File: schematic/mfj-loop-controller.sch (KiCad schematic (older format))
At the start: 35 parts, among them J1 Adafruit ADS1115, J2 Bias Tee, J3 SWR Bridge, J4 DC+12V, U1 AD8032, U2 R-785.0-1.0, U3 TMR3-1212, U4 WeMos_D1_mini, U5 LCC120, U6 LCC120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

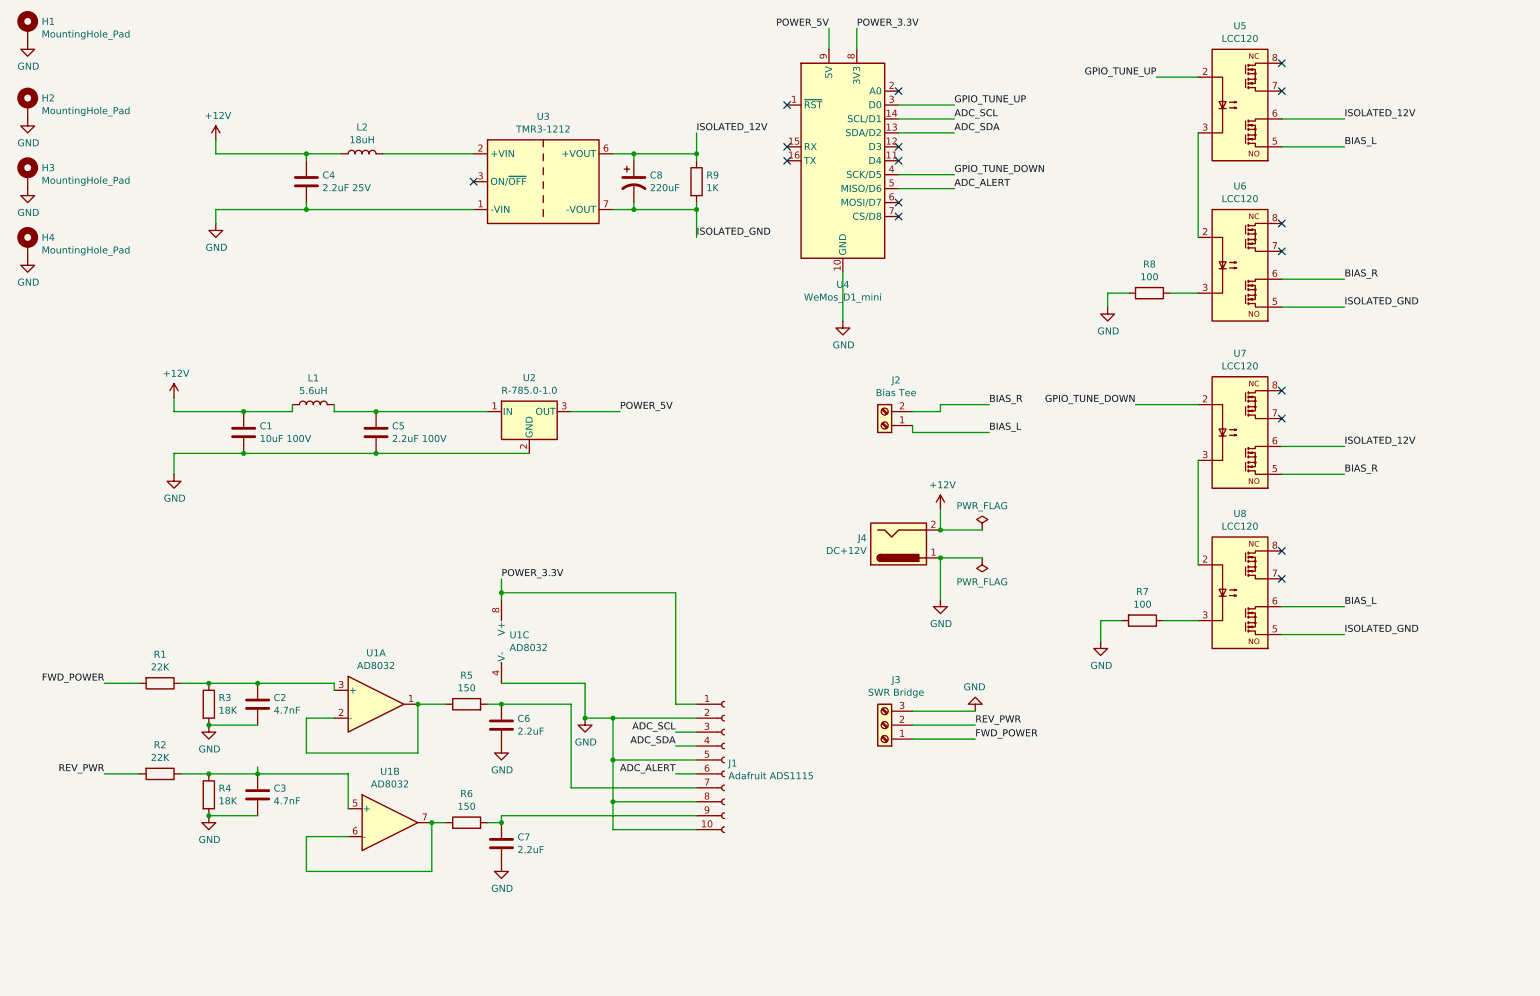
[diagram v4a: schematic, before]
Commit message: Hardware version 1.2.0:
1. Change 12V isolated supply to "low ripple/noise" version (TVN 3-1212).
2. Add/update required filtering to reflect TVN 3-1212 and to further reduce ripple.
3. Reroute isolated section to shorten traces and to use isolated power/ground planes (EMI reduction).
4. Add optional (?) "minimum load" resistors for use if TVN 3-1212 requires them for proper operation while idle/slow tuning.
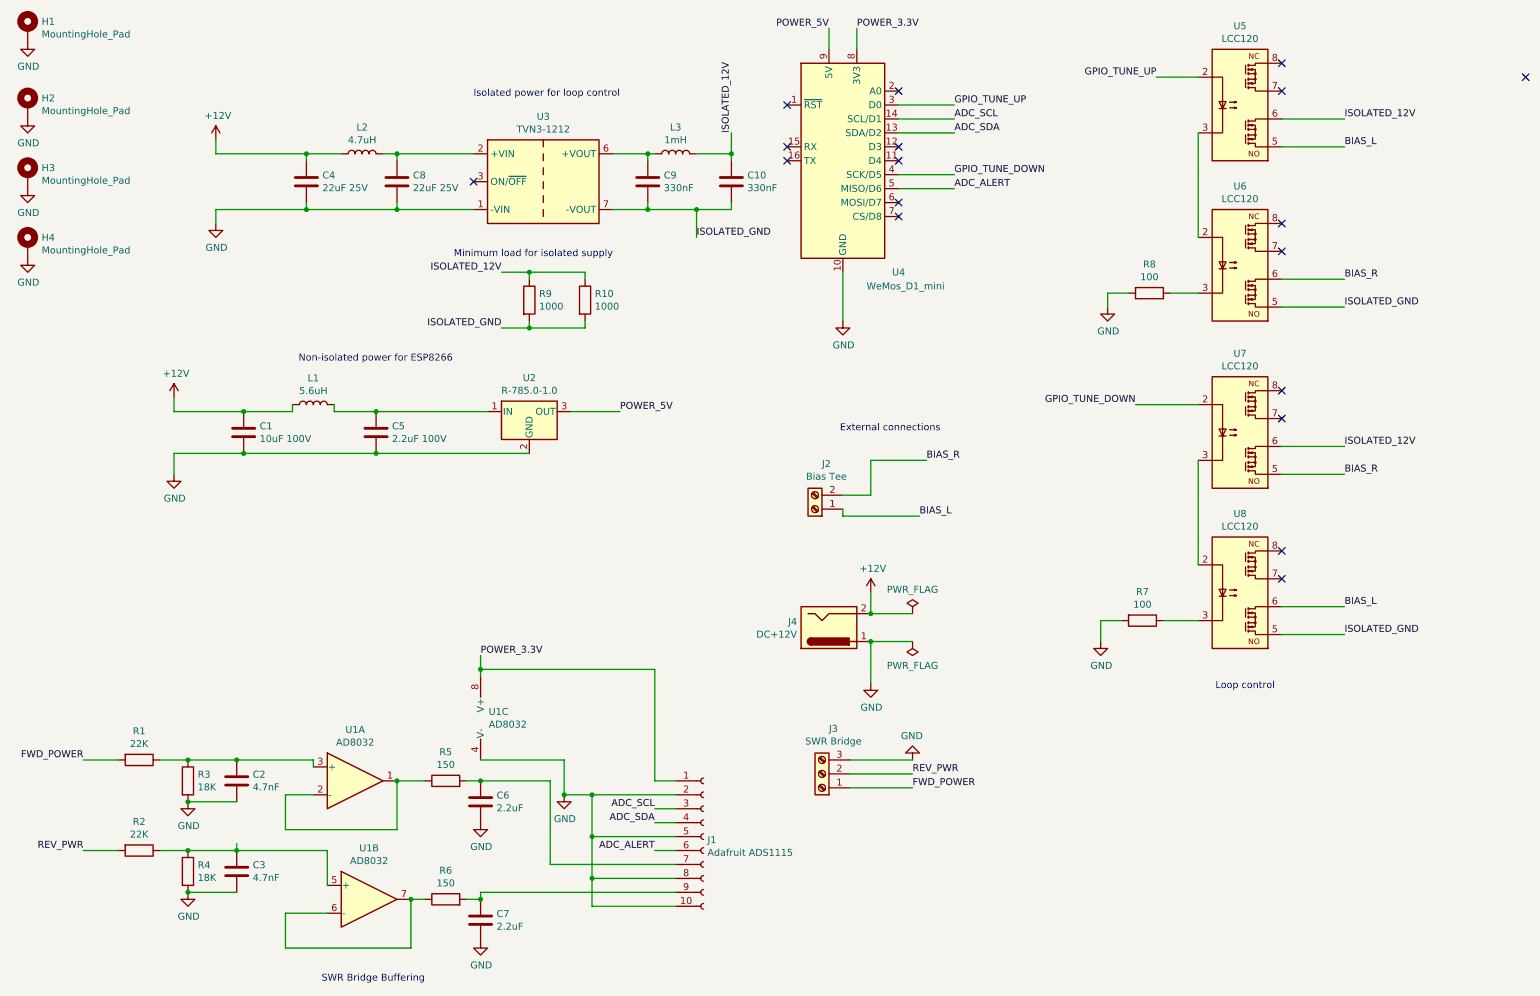
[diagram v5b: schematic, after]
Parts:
- removed C8: 220uF, Capacitor_THT:CP_Radial_D6.3mm_P2.50mm, symbol Device:CP1
- added C10, C9: 330nF, Capacitor_THT:C_Axial_L5.1mm_D3.1mm_P7.50mm_Horizontal, symbol Device:C
- added C8: 22uF 25V, Capacitor_THT:C_Axial_L5.1mm_D3.1mm_P7.50mm_Horizontal, symbol Device:C
- added L3: 1mH, Inductor_THT:L_Axial_L5.3mm_D2.2mm_P10.16mm_Horizontal_Vishay_IM-1, symbol Device:L
- added R10: 1000, Resistor_THT:R_Axial_DIN0207_L6.3mm_D2.5mm_P10.16mm_Horizontal, symbol Device:R
- C4: value 2.2uF 25V -> 22uF 25V
- L2: value 18uH -> 4.7uH
- R9: value 1K -> 1000
- U3: value TMR3-1212 -> TVN3-1212
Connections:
- net GND: now also C8.2
- net ISOLATED_12V: now also C10.1, L3.2, R10.1; no longer U3.6 (+VOUT)
- net ISOLATED_GND: now also C10.2, C9.2, R10.2
- net at L2.2, U3.2 (+VIN): now also C8.1
- new net: C9.1, L3.1, U3.6 (+VOUT)
- no-connect marks 17 -> 18
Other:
- note added: "External connections"
- note added: "Isolated power for loop control"
- note added: "Loop control"
- note added: "Minimum load for isolated supply"
- note added: "Non-isolated power for ESP8266"
- note added: "SWR Bridge Buffering"
- moved on the sheet: C2, C3, C6, C7, J1, J2, J3, J4, R1, R2, R3, R4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
